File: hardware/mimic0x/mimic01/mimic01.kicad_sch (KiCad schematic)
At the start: 33 parts, among them J2 Conn_01x06, J3 Conn_01x03, J5 Conn_01x05, Q1 AO3401A, SW1 TS-1088-AR02016, U1 PY32F071C1BU6TR_DIY

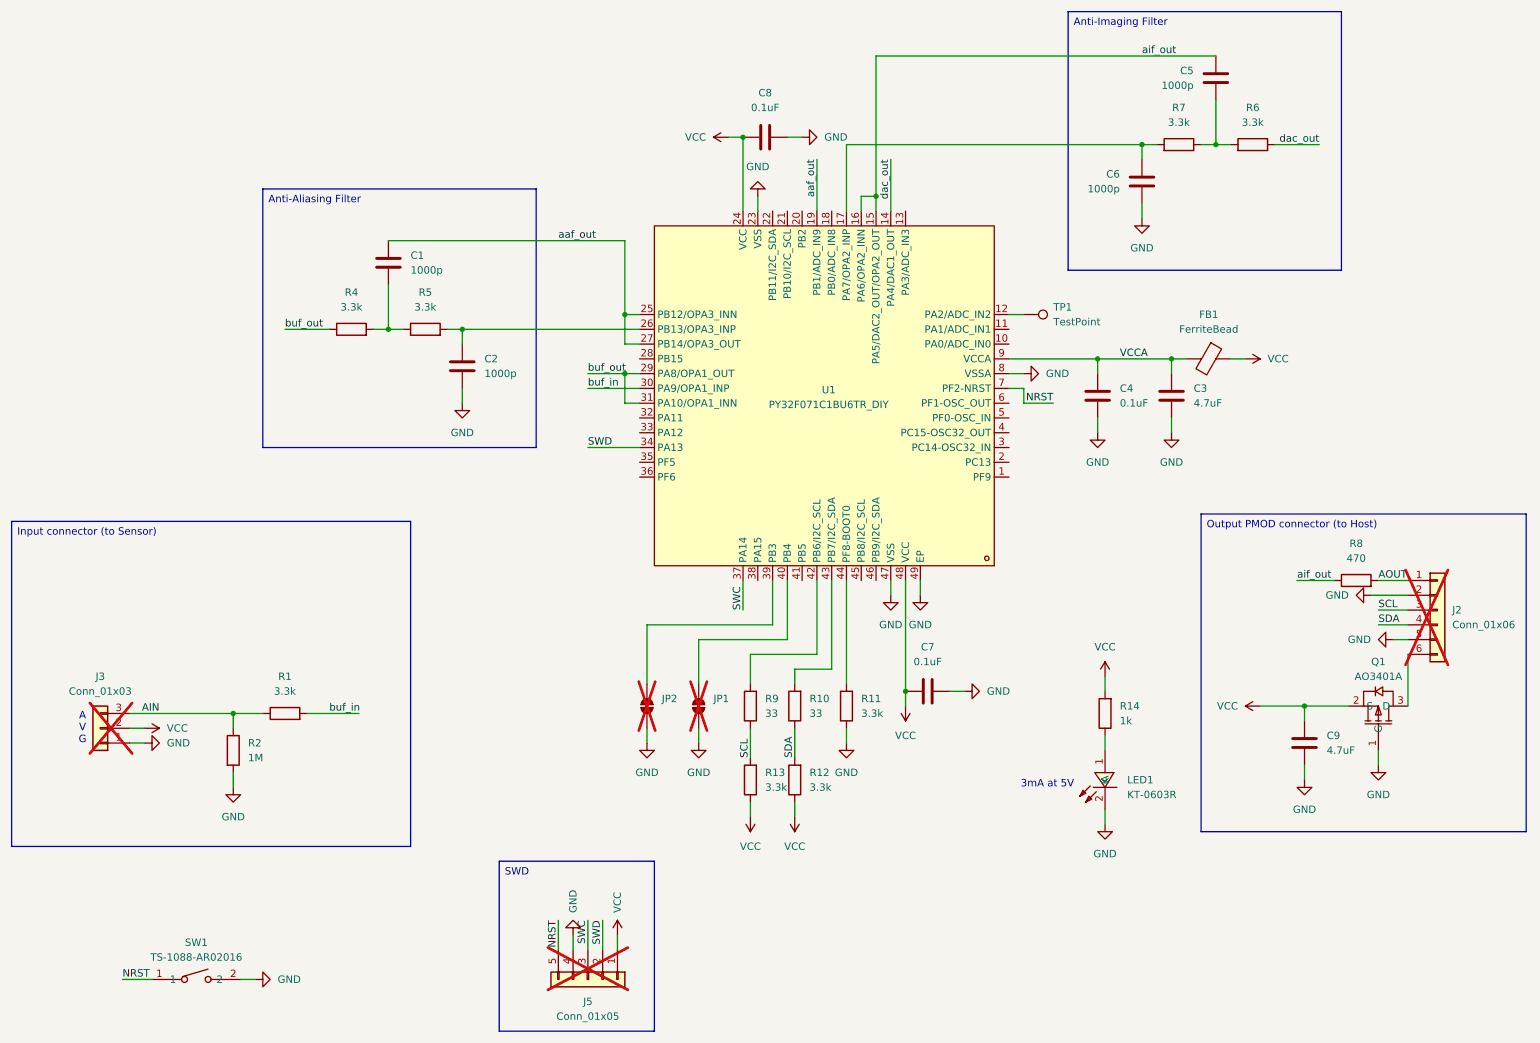
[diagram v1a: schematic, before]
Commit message: Update silk and component values
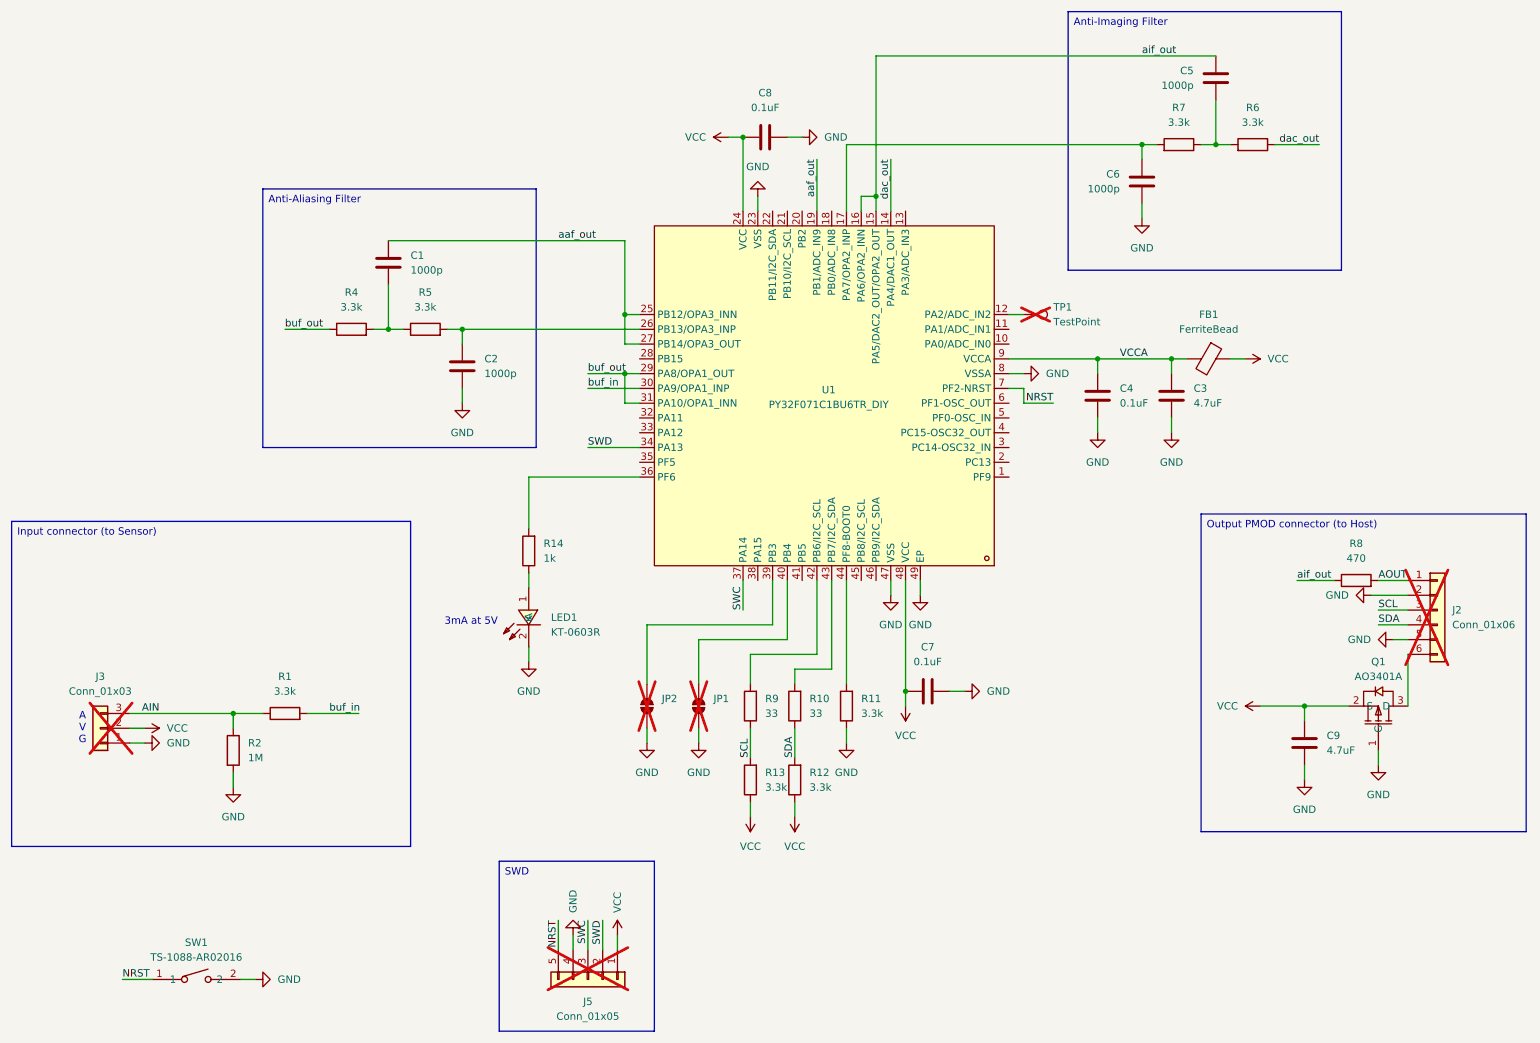
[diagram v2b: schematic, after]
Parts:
- J5: footprint Connector_PinSocket_2.54mm:PinSocket_1x05_P2.54mm_Vertical -> EasyEDA:PinSocket_1x05_P2.54mm_Vertical_DIY
- R14: LCSC Part C173697 -> C11702
- TP1: now not fitted; now left out of the parts list
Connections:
- net VCC: no longer R14.2
- net at U1.36 (PF6): now also R14.2
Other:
- moved on the sheet: LED1, R14
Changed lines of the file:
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@@
 	(text "3mA at 5V"
 		(exclude_from_sim no)
-		(at 198.374 149.352 0)
+		(at 99.314 121.412 0)
 		(effects
 			(font
@@
 	(wire
 		(pts
+			(xy 109.22 96.52) (xy 109.22 105.41)
+		)
+		(stroke
+			(width 0)
+			(type default)
+		)
+	)
+	(wire
+		(pts
 			(xy 199.39 83.82) (xy 194.31 83.82)
 		)
@@
 	(wire
 		(pts
-			(xy 208.28 153.67) (xy 208.28 156.21)
+			(xy 109.22 125.73) (xy 109.22 128.27)
 		)
 		(stroke
@@
 	(wire
 		(pts
-			(xy 208.28 130.81) (xy 208.28 133.35)
+			(xy 128.27 96.52) (xy 109.22 96.52)
 		)
 		(stroke
@@
 	(wire
 		(pts
-			(xy 208.28 140.97) (xy 208.28 143.51)
+			(xy 109.22 113.03) (xy 109.22 115.57)
 		)
 		(stroke
@@
 	(symbol
 		(lib_id "power:GND")
-		(at 208.28 156.21 0)
+		(at 109.22 128.27 0)
 		(unit 1)
 		(exclude_from_sim no)
@@
 		(fields_autoplaced yes)
 		(property "Reference" "#PWR034"
-			(at 208.28 162.56 0)
+			(at 109.22 134.62 0)
 			(effects
 				(font
@@
 		)
 		(property "Value" "GND"
-			(at 208.28 161.29 0)
+			(at 109.22 133.35 0)
 			(effects
 				(font
@@
 		)
 		(property "Footprint" ""
-			(at 208.28 156.21 0)
+			(at 109.22 128.27 0)
 			(effects
 				(font
@@
 		)
 		(property "Datasheet" ""
-			(at 208.28 156.21 0)
+			(at 109.22 128.27 0)
 			(effects
 				(font
@@
 		)
 		(property "Description" "Power symbol creates a global label with name \"GND\" , ground"
-			(at 208.28 156.21 0)
+			(at 109.22 128.27 0)
 			(effects
 				(font
@@
 	)
 	(symbol
-		(lib_id "power:VDD")
-		(at 208.28 130.81 0)
-		(unit 1)
-		(exclude_from_sim no)
-		(in_bom yes)
-		(on_board yes)
-		(dnp no)
-		(fields_autoplaced yes)
-		(property "Reference" "#PWR033"
-			(at 208.28 134.62 0)
-			(effects
-				(font
-					(size 1.27 1.27)
-				)
-				(hide yes)
-			)
-		)
-		(property "Value" "VCC"
-			(at 208.28 125.73 0)
-			(effects
-				(font
-					(size 1.27 1.27)
-				)
-			)
-		)
-		(property "Footprint" ""
-			(at 208.28 130.81 0)
-			(effects
-				(font
-					(size 1.27 1.27)
-				)
-				(hide yes)
-			)
-		)
-		(property "Datasheet" ""
-			(at 208.28 130.81 0)
-			(effects
-				(font
-					(size 1.27 1.27)
-				)
-				(hide yes)
-			)
-		)
-		(property "Description" "Power symbol creates a global label with name \"VDD\""
-			(at 208.28 130.81 0)
-			(effects
-				(font
-					(size 1.27 1.27)
-				)
-				(hide yes)
-			)
-		)
-		(pin "1"
-		)
-		(instances
-			(project "mimic01"
-				(path "/81d4f99a-e1be-4b43-a72c-4e3cf645dbd8"
-					(reference "#PWR033")
-					(unit 1)
-				)
-			)
-		)
-	)
-	(symbol
 		(lib_id "EasyEDA:AO3401A")
 		(at 255.27 138.43 270)
@@
 	(symbol
 		(lib_id "Device:R")
-		(at 208.28 137.16 180)
+		(at 109.22 109.22 180)
 		(unit 1)
 		(exclude_from_sim no)
@@
 		(fields_autoplaced yes)
 		(property "Reference" "R14"
-			(at 210.82 135.8899 0)
+			(at 111.76 107.9499 0)
 			(effects
 				(font
@@
 		)
 		(property "Value" "1k"
-			(at 210.82 138.4299 0)
+			(at 111.76 110.4899 0)
 			(effects
 				(font
@@
 		)
 		(property "Footprint" "Resistor_SMD:R_0402_1005Metric"
-			(at 210.058 137.16 90)
+			(at 110.998 109.22 90)
 			(effects
 				(font
@@
 		)
 		(property "Datasheet" "~"
-			(at 208.28 137.16 0)
+			(at 109.22 109.22 0)
 			(effects
 				(font
@@
 		)
 		(property "Description" "Resistor"
-			(at 208.28 137.16 0)
+			(at 109.22 109.22 0)
 			(effects
 				(font
@@
 			)
 		)
-		(property "LCSC Part" "C173697"
-			(at 208.28 137.16 0)
+		(property "LCSC Part" "C11702"
+			(at 109.22 109.22 0)
 			(effects
 				(font
@@
 	(symbol
 		(lib_id "EasyEDA:KT-0603R")
-		(at 207.01 148.59 90)
+		(at 107.95 120.65 90)
 		(unit 1)
 		(exclude_from_sim no)
@@
 		(fields_autoplaced yes)
 		(property "Reference" "LED1"
-			(at 212.09 148.5899 90)
+			(at 113.03 120.6499 90)
 			(effects
 				(font
@@
 		)
 		(property "Value" "KT-0603R"
-			(at 212.09 151.1299 90)
+			(at 113.03 123.1899 90)
 			(effects
 				(font
@@
 		)
 		(property "Footprint" "EasyEDA:LED-SMD_L1.6-W0.8-R-RD"
-			(at 215.9 148.59 0)
+			(at 116.84 120.65 0)
 			(effects
 				(font
@@
 		)
 		(property "Datasheet" "https://lcsc.com/product-detail/Light-Emitting-Diodes-LED_Red-LED-0603_C2286.html"
-			(at 218.44 148.59 0)
+			(at 119.38 120.65 0)
 			(effects
 				(font
@@
 		)
 		(property "Description" "0603"
-			(at 231.14 148.59 0)
+			(at 132.08 120.65 0)
 			(effects
 				(font
@@
 		)
 		(property "Manufacturer" "KENTO"
-			(at 220.98 148.59 0)
+			(at 121.92 120.65 0)
 			(effects
 				(font
@@
 		)
 		(property "MPN" "KT-0603R"
-			(at 223.52 148.59 0)
+			(at 124.46 120.65 0)
 			(effects
 				(font
@@
 		)
 		(property "LCSC Part" "C2286"
-			(at 226.06 148.59 0)
+			(at 127 120.65 0)
 			(effects
 				(font
@@
 		(unit 1)
 		(exclude_from_sim no)
-		(in_bom yes)
+		(in_bom no)
 		(on_board yes)
-		(dnp no)
+		(dnp yes)
 		(fields_autoplaced yes)
 		(property "Reference" "TP1"
@@
 			)
 		)
-		(property "Footprint" "Connector_PinSocket_2.54mm:PinSocket_1x05_P2.54mm_Vertical"
+		(property "Footprint" "EasyEDA:PinSocket_1x05_P2.54mm_Vertical_DIY"
 			(at 119.38 182.88 0)
 			(effects
